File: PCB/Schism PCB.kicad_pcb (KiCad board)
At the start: 2 copper layers, 176.5 x 225.2 mm, 88 parts, among them J1 USB C Connector, J2 JTAG_TC2030, J3 USB C Connector, J4 USB C Connector, J5 USB C Connector, J6 USB C Connector, SW1 Boot, U1 XC6206, U2 USBLC6-2SC6, U3 RP2040, U4 W25Q128JVS, Y1 12MHz

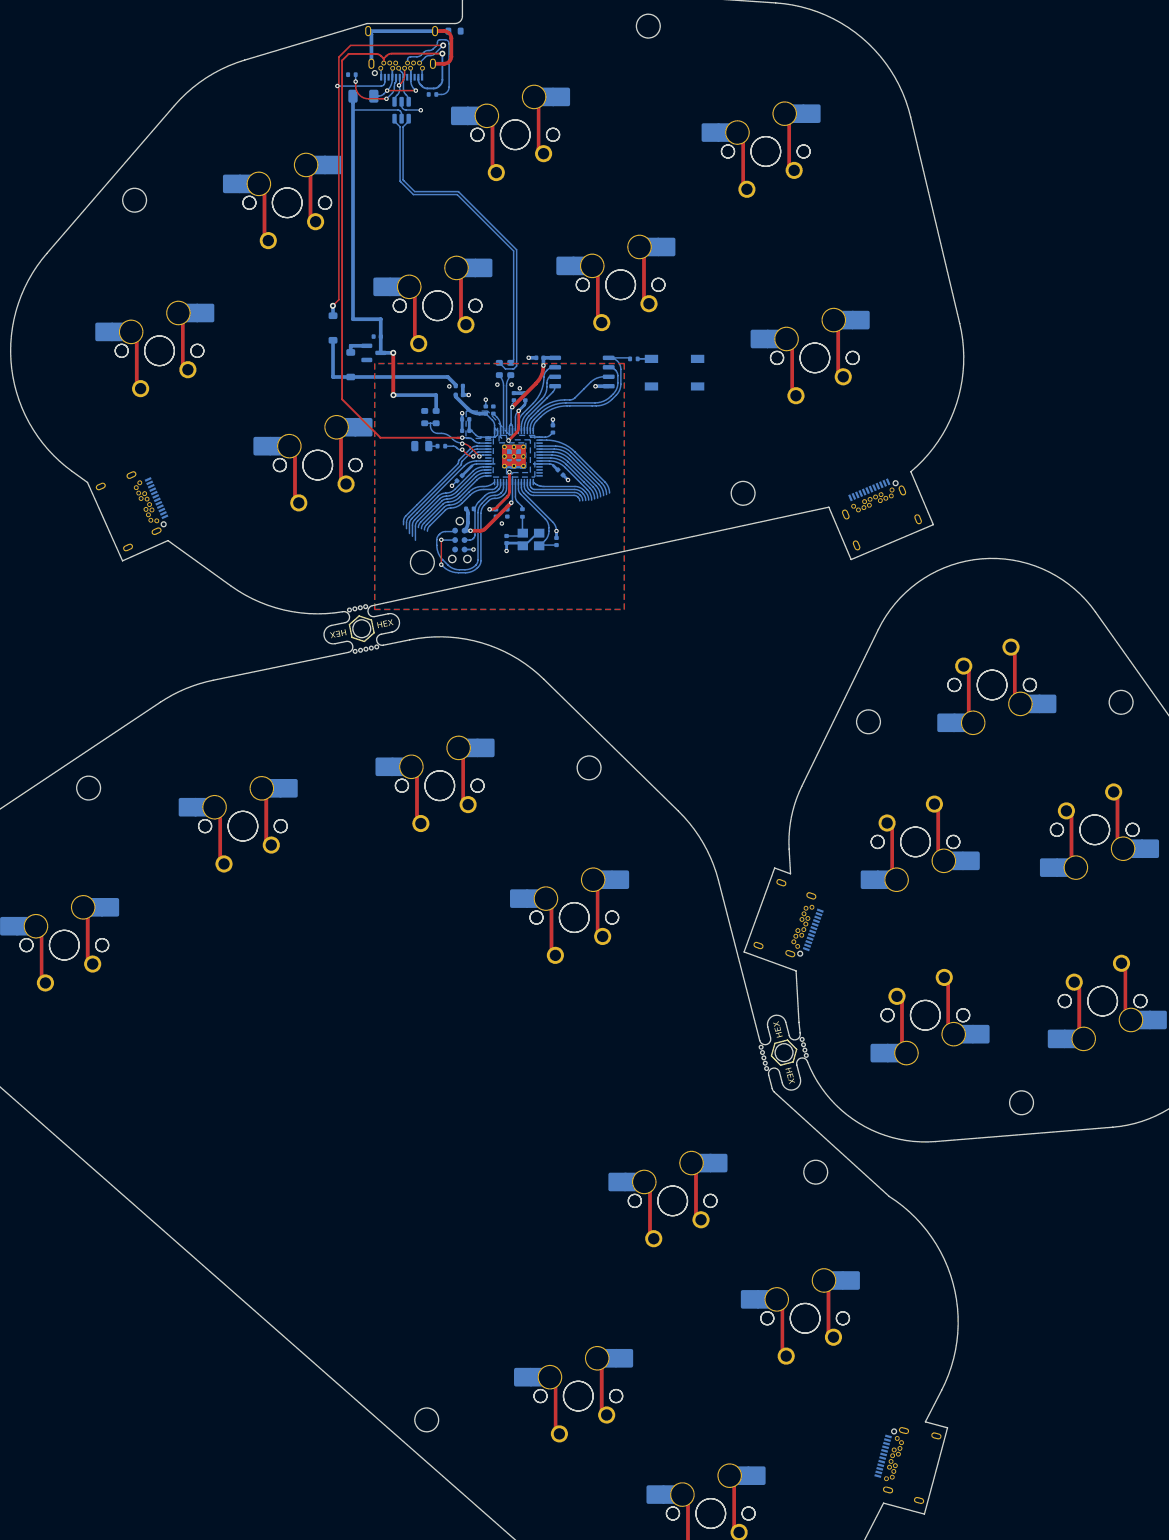
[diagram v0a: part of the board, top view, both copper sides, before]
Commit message: Final schematic and component placement
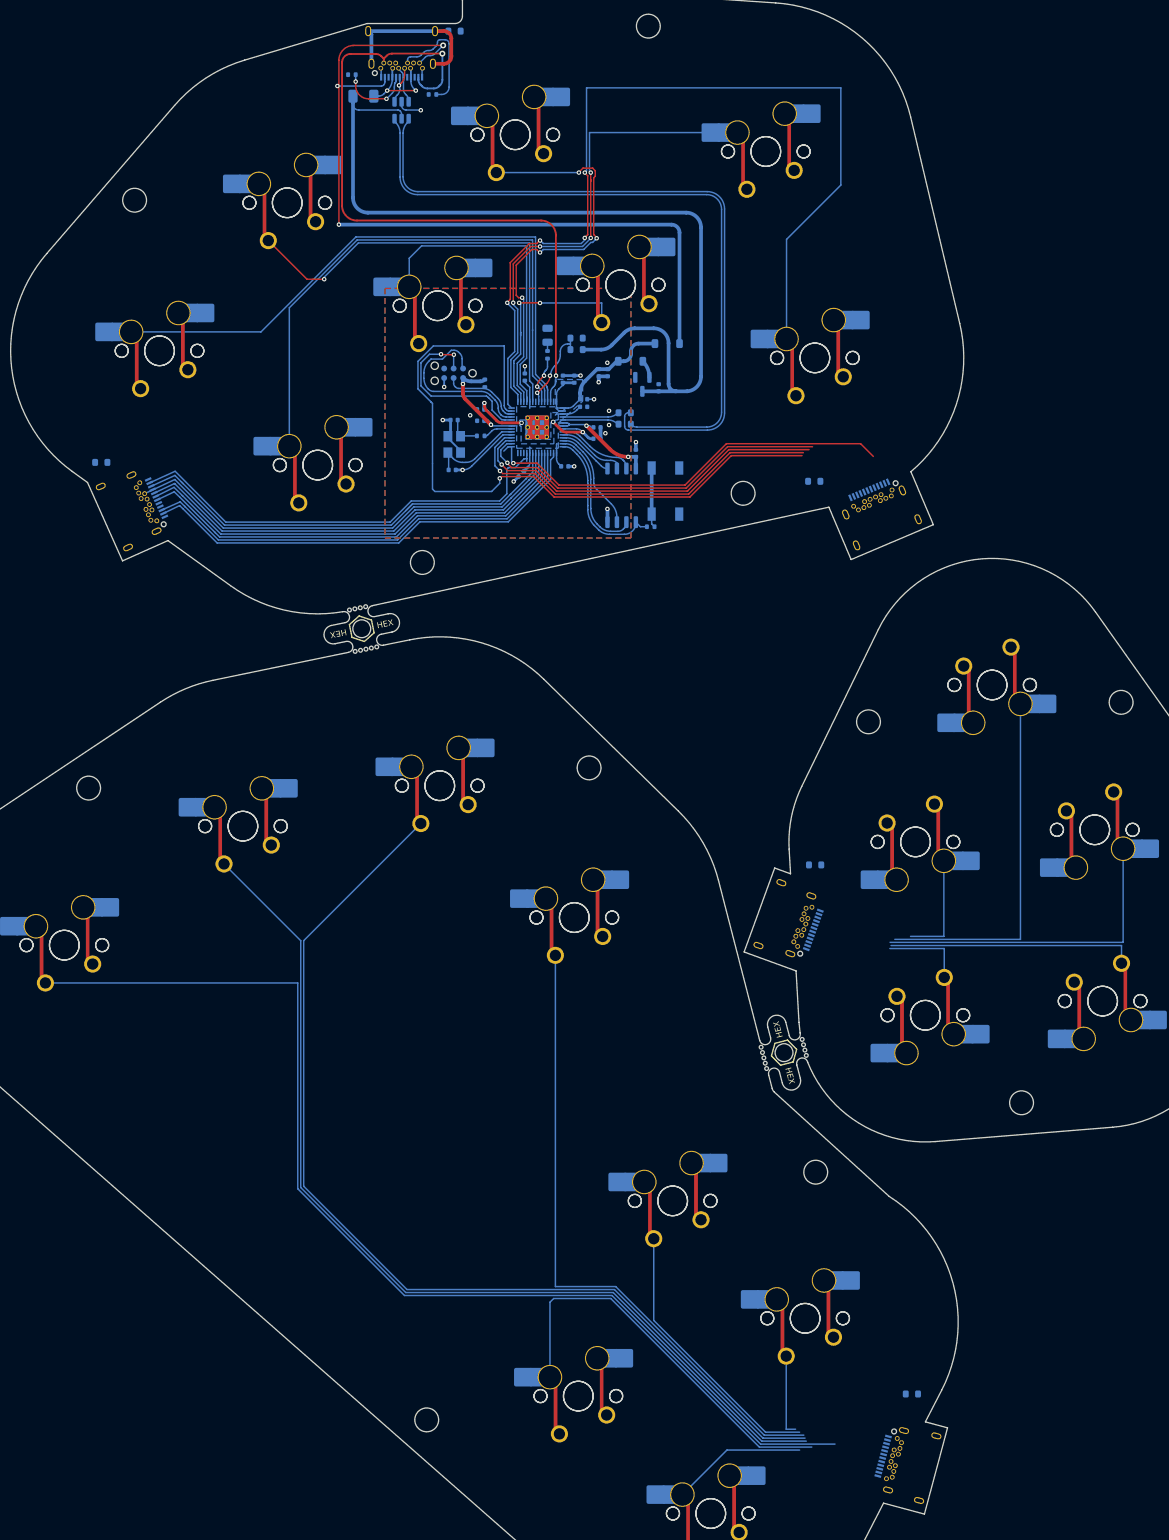
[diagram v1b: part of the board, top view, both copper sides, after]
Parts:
- added R12: 1M, Resistor_SMD:R_0603_1608Metric, B.Cu at (154.1, 208.8)
- added R13: 1M, Resistor_SMD:R_0603_1608Metric, B.Cu at (45.2, 83.6)
- added R14: 1M, Resistor_SMD:R_0603_1608Metric, B.Cu at (141.1, 137.7)
- added R15: 1M, Resistor_SMD:R_0603_1608Metric, B.Cu at (141.0, 86.2)
- MB5: value 5.5mm -> MouseBites
- MB6: renamed from MB5; value 5.5mm -> MouseBites
- moved D2 44.9 mm to (121.2, 67.7), turned to 0 degrees
- moved C2 38.4 mm to (120.1, 73.6), turned to -90 degrees
- moved D1 37.6 mm to (116.3, 70.1), turned to 0 degrees
- moved U1 36.3 mm to (117.9, 73.2), turned to -90 degrees
- moved R6 23.0 mm to (109.0, 66.9), turned to 0 degrees
- moved R10 22.7 mm to (119.0, 92.3)
- moved D3 22.5 mm to (105.1, 66.6), turned to -90 degrees
- moved J2 22.4 mm to (92.5, 71.7), turned to 180 degrees
- moved R5 20.9 mm to (109.0, 68.5), turned to 180 degrees
- moved C9 20.0 mm to (113.2, 71.6), turned to -90 degrees
- moved C1 19.0 mm to (112.0, 71.6), turned to 90 degrees
- moved R4 18.8 mm to (105.1, 69.2), turned to 90 degrees
- moved C3 18.2 mm to (117.0, 82.4), turned to 90 degrees
- moved R9 17.8 mm to (115.5, 77.0), turned to 180 degrees
- moved C8 17.5 mm to (92.6, 77.9), turned to 0 degrees
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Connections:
- J3 pad A1: Net-(J3-GND-PadA1) -> GND
- J3 pad A10: unconnected-(J3-RX2--PadA10) -> M2_2
- J3 pad A11: unconnected-(J3-RX2+-PadA11) -> M3_2
- J3 pad A12: Net-(J3-GND-PadA1) -> GND
- J3 pad A2: unconnected-(J3-TX1+-PadA2) -> START_2
- J3 pad A3: unconnected-(J3-TX1--PadA3) -> RIGHT_2
- J3 pad A4: Net-(J3-VBUS-PadA4) -> M1_2
- J3 pad A6: unconnected-(J3-D+-PadA6) -> DOWN_2
- J3 pad A7: unconnected-(J3-D--PadA7) -> LEFT_2
- J3 pad A8: unconnected-(J3-SBU1-PadA8) -> L_2
- J3 pad A9: Net-(J3-VBUS-PadA4) -> M1_2
- J3 pad B1: Net-(J3-GND-PadA1) -> GND
- J3 pad B10: unconnected-(J3-RX1--PadB10) -> M2_2
- J3 pad B11: unconnected-(J3-RX1+-PadB11) -> M3_2
- J3 pad B12: Net-(J3-GND-PadA1) -> GND
- J3 pad B2: unconnected-(J3-TX2+-PadB2) -> START_2
- J3 pad B3: unconnected-(J3-TX2--PadB3) -> RIGHT_2
- J3 pad B4: Net-(J3-VBUS-PadA4) -> M1_2
- J3 pad B6: unconnected-(J3-D+-PadB6) -> DOWN_2
- J3 pad B7: unconnected-(J3-D--PadB7) -> LEFT_2
- J3 pad B8: unconnected-(J3-SBU2-PadB8) -> L_2
- J3 pad B9: Net-(J3-VBUS-PadA4) -> M1_2
- J3 pad S1: unconnected-(J3-SHIELD-PadS1) -> Net-(J3-SHIELD)
- J4 pad A1: Net-(J4-GND-PadA1) -> GND
- J4 pad A10: unconnected-(J4-RX2--PadA10) -> C_DN_2
- J4 pad A11: unconnected-(J4-RX2+-PadA11) -> C_RT_2
- J4 pad A12: Net-(J4-GND-PadA1) -> GND
- J4 pad A2: unconnected-(J4-TX1+-PadA2) -> C_UP_2
- J4 pad A4: Net-(J4-VBUS-PadA4) -> unconnected-(J4-VBUS-PadA4)
- J4 pad A6: unconnected-(J4-D+-PadA6) -> C_LT_2
- J4 pad A7: unconnected-(J4-D--PadA7) -> A_2
- J4 pad A9: Net-(J4-VBUS-PadA4) -> unconnected-(J4-VBUS-PadA4)
- J4 pad B1: Net-(J4-GND-PadA1) -> GND
- J4 pad B10: unconnected-(J4-RX1--PadB10) -> C_DN_2
- J4 pad B11: unconnected-(J4-RX1+-PadB11) -> C_RT_2
- J4 pad B12: Net-(J4-GND-PadA1) -> GND
- J4 pad B2: unconnected-(J4-TX2+-PadB2) -> C_UP_2
- J4 pad B4: Net-(J4-VBUS-PadA4) -> unconnected-(J4-VBUS-PadA4)
- J4 pad B6: unconnected-(J4-D+-PadB6) -> C_LT_2
- J4 pad B7: unconnected-(J4-D--PadB7) -> A_2
- J4 pad B9: Net-(J4-VBUS-PadA4) -> unconnected-(J4-VBUS-PadA4)
- J4 pad S1: unconnected-(J4-SHIELD-PadS1) -> Net-(J4-SHIELD)
- J5 pad A1: Net-(J5-GND-PadA1) -> GND
- J5 pad A10: unconnected-(J5-RX2--PadA10) -> M2
- J5 pad A11: unconnected-(J5-RX2+-PadA11) -> M3
- J5 pad A12: Net-(J5-GND-PadA1) -> GND
- J5 pad A2: unconnected-(J5-TX1+-PadA2) -> START
- J5 pad A3: unconnected-(J5-TX1--PadA3) -> RIGHT
- J5 pad A4: Net-(J5-VBUS-PadA4) -> M1
- J5 pad A6: unconnected-(J5-D+-PadA6) -> DOWN
- J5 pad A7: unconnected-(J5-D--PadA7) -> LEFT
- J5 pad A8: unconnected-(J5-SBU1-PadA8) -> L
- J5 pad A9: Net-(J5-VBUS-PadA4) -> M1
- J5 pad B1: Net-(J5-GND-PadA1) -> GND
- J5 pad B10: unconnected-(J5-RX1--PadB10) -> M2
- J5 pad B11: unconnected-(J5-RX1+-PadB11) -> M3
- J5 pad B12: Net-(J5-GND-PadA1) -> GND
- J5 pad B2: unconnected-(J5-TX2+-PadB2) -> START
- J5 pad B3: unconnected-(J5-TX2--PadB3) -> RIGHT
- J5 pad B4: Net-(J5-VBUS-PadA4) -> M1
- J5 pad B6: unconnected-(J5-D+-PadB6) -> DOWN
- J5 pad B7: unconnected-(J5-D--PadB7) -> LEFT
- J5 pad B8: unconnected-(J5-SBU2-PadB8) -> L
- J5 pad B9: Net-(J5-VBUS-PadA4) -> M1
- J5 pad S1: unconnected-(J5-SHIELD-PadS1) -> Net-(J5-SHIELD)
- J6 pad A1: Net-(J6-GND-PadA1) -> GND
- J6 pad A10: unconnected-(J6-RX2--PadA10) -> C_DN
- J6 pad A11: unconnected-(J6-RX2+-PadA11) -> C_RT
- J6 pad A12: Net-(J6-GND-PadA1) -> GND
- J6 pad A2: unconnected-(J6-TX1+-PadA2) -> C_UP
- J6 pad A4: Net-(J6-VBUS-PadA4) -> unconnected-(J6-VBUS-PadA4)
- J6 pad A6: unconnected-(J6-D+-PadA6) -> C_LT
- J6 pad A7: unconnected-(J6-D--PadA7) -> A
- J6 pad A9: Net-(J6-VBUS-PadA4) -> unconnected-(J6-VBUS-PadA4)
- J6 pad B1: Net-(J6-GND-PadA1) -> GND
- J6 pad B10: unconnected-(J6-RX1--PadB10) -> C_DN
- J6 pad B11: unconnected-(J6-RX1+-PadB11) -> C_RT
- J6 pad B12: Net-(J6-GND-PadA1) -> GND
- J6 pad B2: unconnected-(J6-TX2+-PadB2) -> C_UP
- J6 pad B4: Net-(J6-VBUS-PadA4) -> unconnected-(J6-VBUS-PadA4)
- J6 pad B6: unconnected-(J6-D+-PadB6) -> C_LT
- J6 pad B7: unconnected-(J6-D--PadB7) -> A
- J6 pad B9: Net-(J6-VBUS-PadA4) -> unconnected-(J6-VBUS-PadA4)
- J6 pad S1: unconnected-(J6-SHIELD-PadS1) -> Net-(J6-SHIELD)
- MX1 pad 1: Net-(MX1-Pad1) -> L_2
- MX1 pad 2: Net-(MX1-Pad2) -> GND
- MX10 pad 1: Net-(MX10-Pad1) -> GND
- MX10 pad 2: Net-(MX10-Pad2) -> M1_2
- MX11 pad 1: Net-(MX11-Pad1) -> GND
- MX11 pad 2: Net-(MX11-Pad2) -> M3_2
- MX12 pad 1: Net-(MX11-Pad2) -> M3_2
- MX12 pad 2: Net-(MX11-Pad1) -> GND
- MX13 pad 1: Net-(MX13-Pad1) -> M2_2
- MX13 pad 2: Net-(MX13-Pad2) -> GND
- MX14 pad 1: Net-(MX13-Pad2) -> GND
- MX14 pad 2: Net-(MX13-Pad1) -> M2_2
- MX15 pad 1: Net-(MX15-Pad1) -> GND
- MX15 pad 2: Net-(MX15-Pad2) -> START_2
- MX16 pad 1: Net-(MX15-Pad2) -> START_2
- MX16 pad 2: Net-(MX15-Pad1) -> GND
- MX17 pad 1: Net-(MX17-Pad1) -> GND
- MX17 pad 2: Net-(MX17-Pad2) -> B
- MX18 pad 1: Net-(MX17-Pad2) -> B
- MX18 pad 2: Net-(MX17-Pad1) -> GND
- MX19 pad 1: Net-(MX19-Pad1) -> GND
- MX19 pad 2: Net-(MX19-Pad2) -> X
- MX2 pad 1: Net-(MX1-Pad2) -> GND
- MX2 pad 2: Net-(MX1-Pad1) -> L_2
- MX20 pad 1: Net-(MX19-Pad2) -> X
- MX20 pad 2: Net-(MX19-Pad1) -> GND
- MX21 pad 1: Net-(MX21-Pad1) -> Z
- MX21 pad 2: Net-(MX21-Pad2) -> GND
- MX22 pad 1: Net-(MX21-Pad2) -> GND
- MX22 pad 2: Net-(MX21-Pad1) -> Z
- MX23 pad 1: Net-(MX23-Pad1) -> GND
- MX23 pad 2: Net-(MX23-Pad2) -> UP
- MX24 pad 1: Net-(MX23-Pad2) -> UP
- MX24 pad 2: Net-(MX23-Pad1) -> GND
- MX25 pad 1: Net-(MX25-Pad1) -> GND
- MX25 pad 2: Net-(MX25-Pad2) -> R
- MX26 pad 1: Net-(MX25-Pad2) -> R
- MX26 pad 2: Net-(MX25-Pad1) -> GND
- MX27 pad 1: Net-(MX27-Pad1) -> GND
- MX27 pad 2: Net-(MX27-Pad2) -> Y
- MX28 pad 1: Net-(MX27-Pad2) -> Y
- MX28 pad 2: Net-(MX27-Pad1) -> GND
- MX29 pad 1: Net-(MX29-Pad1) -> GND
- MX29 pad 2: Net-(MX29-Pad2) -> LS
- MX3 pad 1: Net-(MX3-Pad1) -> LEFT_2
- MX3 pad 2: Net-(MX3-Pad2) -> GND
- MX30 pad 1: Net-(MX29-Pad2) -> LS
- MX30 pad 2: Net-(MX29-Pad1) -> GND
- MX31 pad 1: Net-(MX31-Pad1) -> GND
- MX31 pad 2: Net-(MX31-Pad2) -> MS
- MX32 pad 1: Net-(MX31-Pad2) -> MS
- MX32 pad 2: Net-(MX31-Pad1) -> GND
- MX33 pad 1: Net-(MX33-Pad1) -> GND
- MX33 pad 2: Net-(MX33-Pad2) -> C_DN_2
- MX34 pad 1: Net-(MX33-Pad2) -> C_DN_2
- MX34 pad 2: Net-(MX33-Pad1) -> GND
- MX35 pad 1: Net-(MX35-Pad1) -> A_2
- MX35 pad 2: Net-(MX35-Pad2) -> GND
- MX36 pad 1: Net-(MX35-Pad2) -> GND
- MX36 pad 2: Net-(MX35-Pad1) -> A_2
- MX37 pad 1: Net-(MX37-Pad1) -> C_RT_2
- MX37 pad 2: Net-(MX37-Pad2) -> GND
- MX38 pad 1: Net-(MX37-Pad2) -> GND
- MX38 pad 2: Net-(MX37-Pad1) -> C_RT_2
- MX39 pad 1: Net-(MX39-Pad1) -> C_LT_2
- MX39 pad 2: Net-(MX39-Pad2) -> GND
- MX4 pad 1: Net-(MX3-Pad2) -> GND
- MX4 pad 2: Net-(MX3-Pad1) -> LEFT_2
- MX40 pad 1: Net-(MX39-Pad2) -> GND
- MX40 pad 2: Net-(MX39-Pad1) -> C_LT_2
- MX41 pad 1: Net-(MX41-Pad1) -> C_UP_2
- MX41 pad 2: Net-(MX41-Pad2) -> GND
- MX42 pad 1: Net-(MX41-Pad2) -> GND
- MX42 pad 2: Net-(MX41-Pad1) -> C_UP_2
- MX5 pad 1: Net-(MX5-Pad1) -> GND
- MX5 pad 2: Net-(MX5-Pad2) -> DOWN_2
- MX6 pad 1: Net-(MX5-Pad2) -> DOWN_2
- MX6 pad 2: Net-(MX5-Pad1) -> GND
- MX7 pad 1: Net-(MX7-Pad1) -> GND
- MX7 pad 2: Net-(MX7-Pad2) -> RIGHT_2
- MX8 pad 1: Net-(MX7-Pad2) -> RIGHT_2
- MX8 pad 2: Net-(MX7-Pad1) -> GND
- MX9 pad 1: Net-(MX10-Pad2) -> M1_2
- MX9 pad 2: Net-(MX10-Pad1) -> GND
- U3 pad 11: unconnected-(U3-GPIO8-Pad11) -> M3
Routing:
- net GND: track 49.4 -> 220.6 mm
- net L_2: track 0.00 -> 156.1 mm
- net DOWN_2: track 0.00 -> 144.8 mm
- net LEFT_2: track 0.00 -> 137.9 mm
- net UP: track 11.9 -> 132.2 mm, vias 0 -> 4
- net RIGHT_2: track 0.00 -> 94.3 mm
- net C_RT: track 12.3 -> 94.4 mm, vias 0 -> 1
- net R: track 16.3 -> 90.5 mm
- net B: track 16.2 -> 85.7 mm
- net M1_2: track 0.00 -> 61.9 mm
- net M3: track 0.00 -> 60.4 mm
- net MS: track 11.9 -> 72.0 mm, vias 0 -> 4
- net +5V: track 62.3 -> 120.5 mm, vias 2 -> 0
- net C_DN_2: track 0.00 -> 56.7 mm
- net Y: track 15.5 -> 69.1 mm, vias 0 -> 1
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
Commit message: Almost done with the routing
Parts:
- moved R14 15.7 mm to (137.6, 153.0), turned to 70 degrees
- moved R15 8.41 mm to (148.4, 82.2), turned to -157 degrees
- moved R13 5.55 mm to (39.7, 83.9), turned to -65.9 degrees
- moved R12 4.68 mm to (149.8, 210.6)
- moved C12 4.15 mm to (105.8, 75.1)
- moved D1 4.15 mm to (112.1, 70.0)
- moved MB5 4.15 mm to (75.5, 103.3)
- moved MX29 4.15 mm to (96.7, 39.6)
- moved MX30 4.15 mm to (96.7, 39.6)
- moved C4 4.15 mm to (105.8, 76.2)
- moved C5 4.15 mm to (107.6, 80.4)
- moved D3 4.15 mm to (101.0, 66.5)
- moved R5 4.15 mm to (104.9, 68.5)
- moved D2 4.15 mm to (117.1, 67.7)
- moved J6 4.15 mm to (147.4, 94.7)
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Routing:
- net C_RT_2: track 19.3 -> 49.1 mm, vias 0 -> 3
- net M3_2: track 44.9 -> 73.2 mm, vias 0 -> 1
- net C_DN_2: track 56.7 -> 82.8 mm, vias 0 -> 2
- net C_DN: track 50.6 -> 76.2 mm, vias 1 -> 2
- net C_UP_2: track 41.5 -> 66.7 mm, vias 0 -> 1
- net C_RT: track 94.4 -> 119.2 mm, vias 1 -> 3
- net Net-(J6-SHIELD): track 0.00 -> 23.6 mm
- net Net-(J4-SHIELD): track 0.00 -> 23.6 mm
- net START_2: track 19.2 -> 41.6 mm, vias 0 -> 1
- net Net-(J5-SHIELD): track 0.00 -> 21.7 mm
- net M2_2: track 26.4 -> 47.7 mm, vias 0 -> 2
- net Net-(J3-SHIELD): track 0.00 -> 21.2 mm
- net L_2: track 156.1 -> 175.2 mm, vias 0 -> 2
- net RIGHT_2: track 94.3 -> 112.4 mm, vias 0 -> 1
- net C_UP: track 56.2 -> 73.7 mm, vias 1 -> 2
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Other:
- board text added: "J5"
